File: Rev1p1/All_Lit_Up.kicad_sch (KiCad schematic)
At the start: 81 parts, among them U1 MCP1640BMC, U2 TLC555xPW

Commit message: Improved 1p1 Design
Cleaned up design, removed DFN for SOIC. added BOM, Schematic, & Step Files. reduced size to 100mm x 100mm. improved traces & Vias.
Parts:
- removed U1: MCP1640BMC, Package_DFN_QFN:DFN-8-1EP_3x2mm_P0.5mm_EP1.75x1.45mm, symbol ERW_Power:MCP1640BMC
- added G1: LOGO, ERW_LOGO:RuralguruProjects_HEX_2000, symbol ERW_LOGO:LOGO
- added G2: Phillip_LOGO, ERW_LOGO:PJ_LOGO_1p5l, symbol ERW_LOGO:Phillip_LOGO
- added G3: Logo_Open_Hardware_Small, Symbol:OSHW-Symbol_6.7x6mm_SilkScreen, symbol Graphic:Logo_Open_Hardware_Small
- added U1: MCP1640Bx-xCHY, Package_TO_SOT_SMD:SOT-23-6, symbol Regulator_Switching:MCP1640Bx-xCHY
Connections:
- net GND: now also U1.2 (GND)
- net PWR_EN: now also U1.3 (EN)
- net SWITCHER: now also U1.1 (SW)
- net VCC: now also U1.5 (V_{OUT})
- net V_{BAT}: now also U1.6 (V_{IN})
- net VFB renamed V_{FB}
- net V_{FB}: now also U1.4 (V_{FB})
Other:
- moved on the sheet: C1, C10, C13, C14, C16, C17, C2, C21, C23, C24, C25, C26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

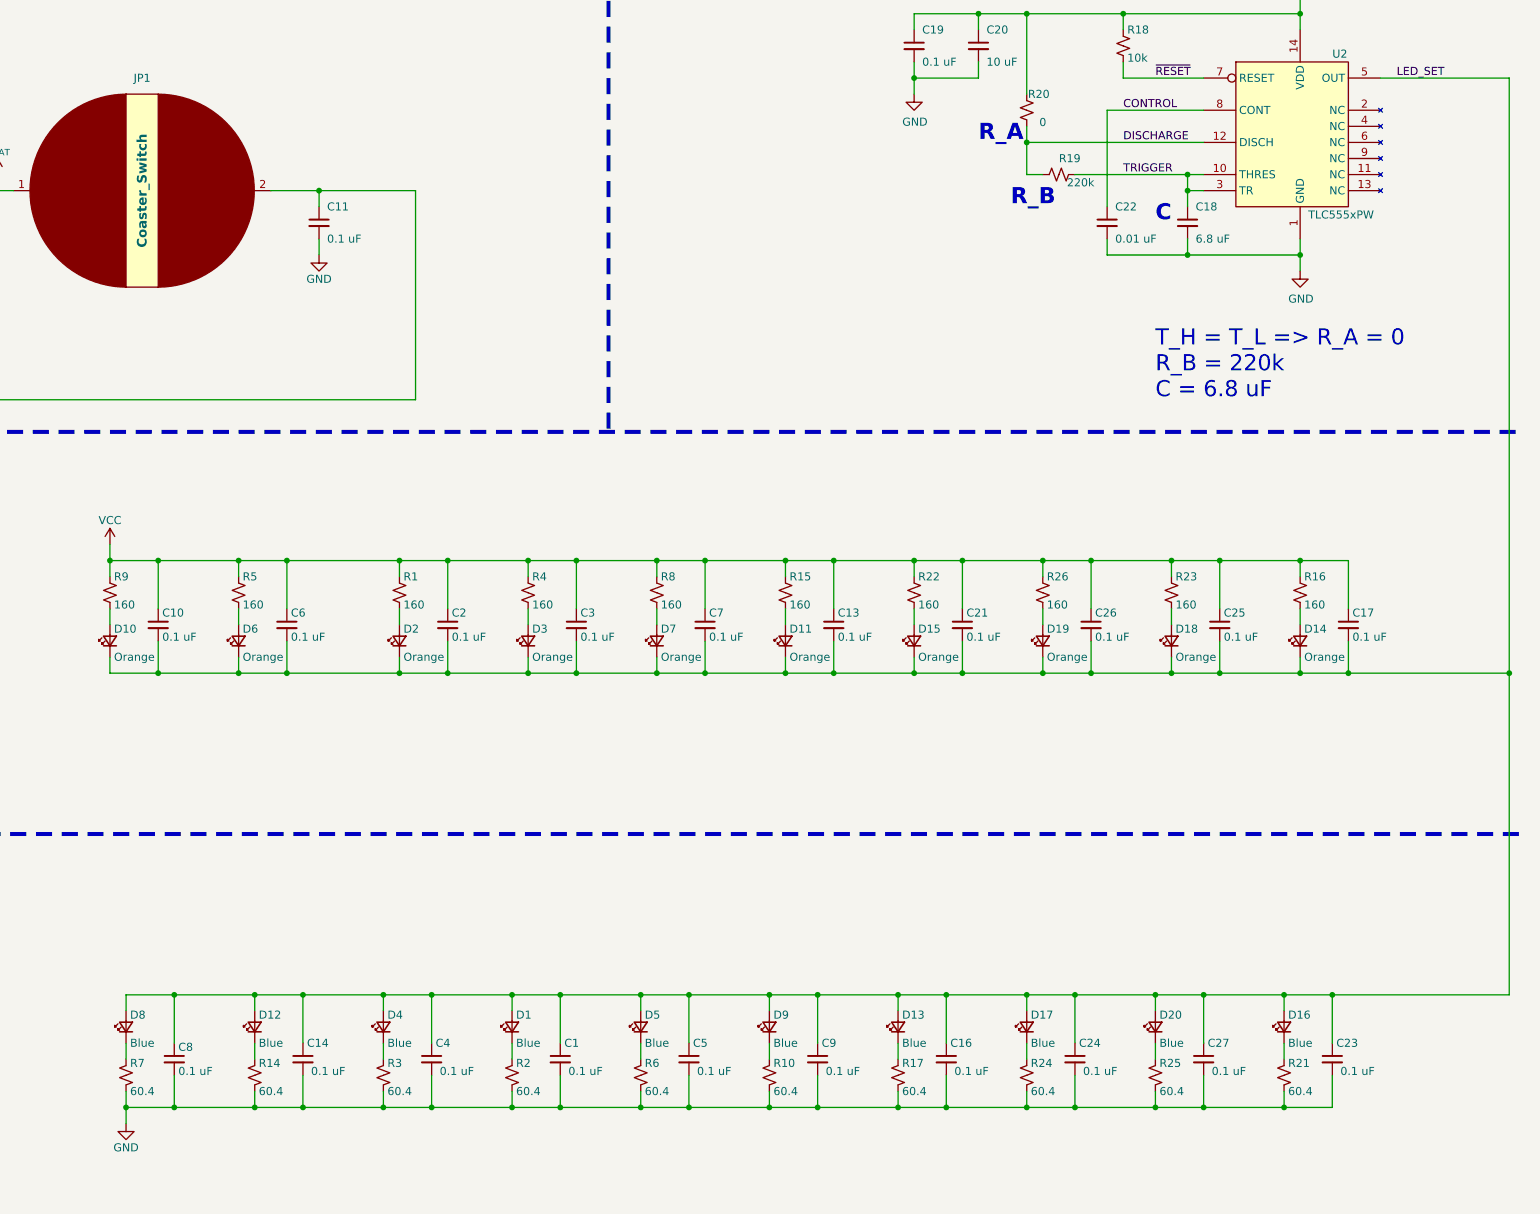
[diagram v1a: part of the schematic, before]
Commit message: Update to working model
Change LEDs to used Value, Correct to 1k, change resistor values to used. Add LED choice and orientation with silk. correct silk for 1 LED Cap combo. update gbrs. update output documents. Added iBOM
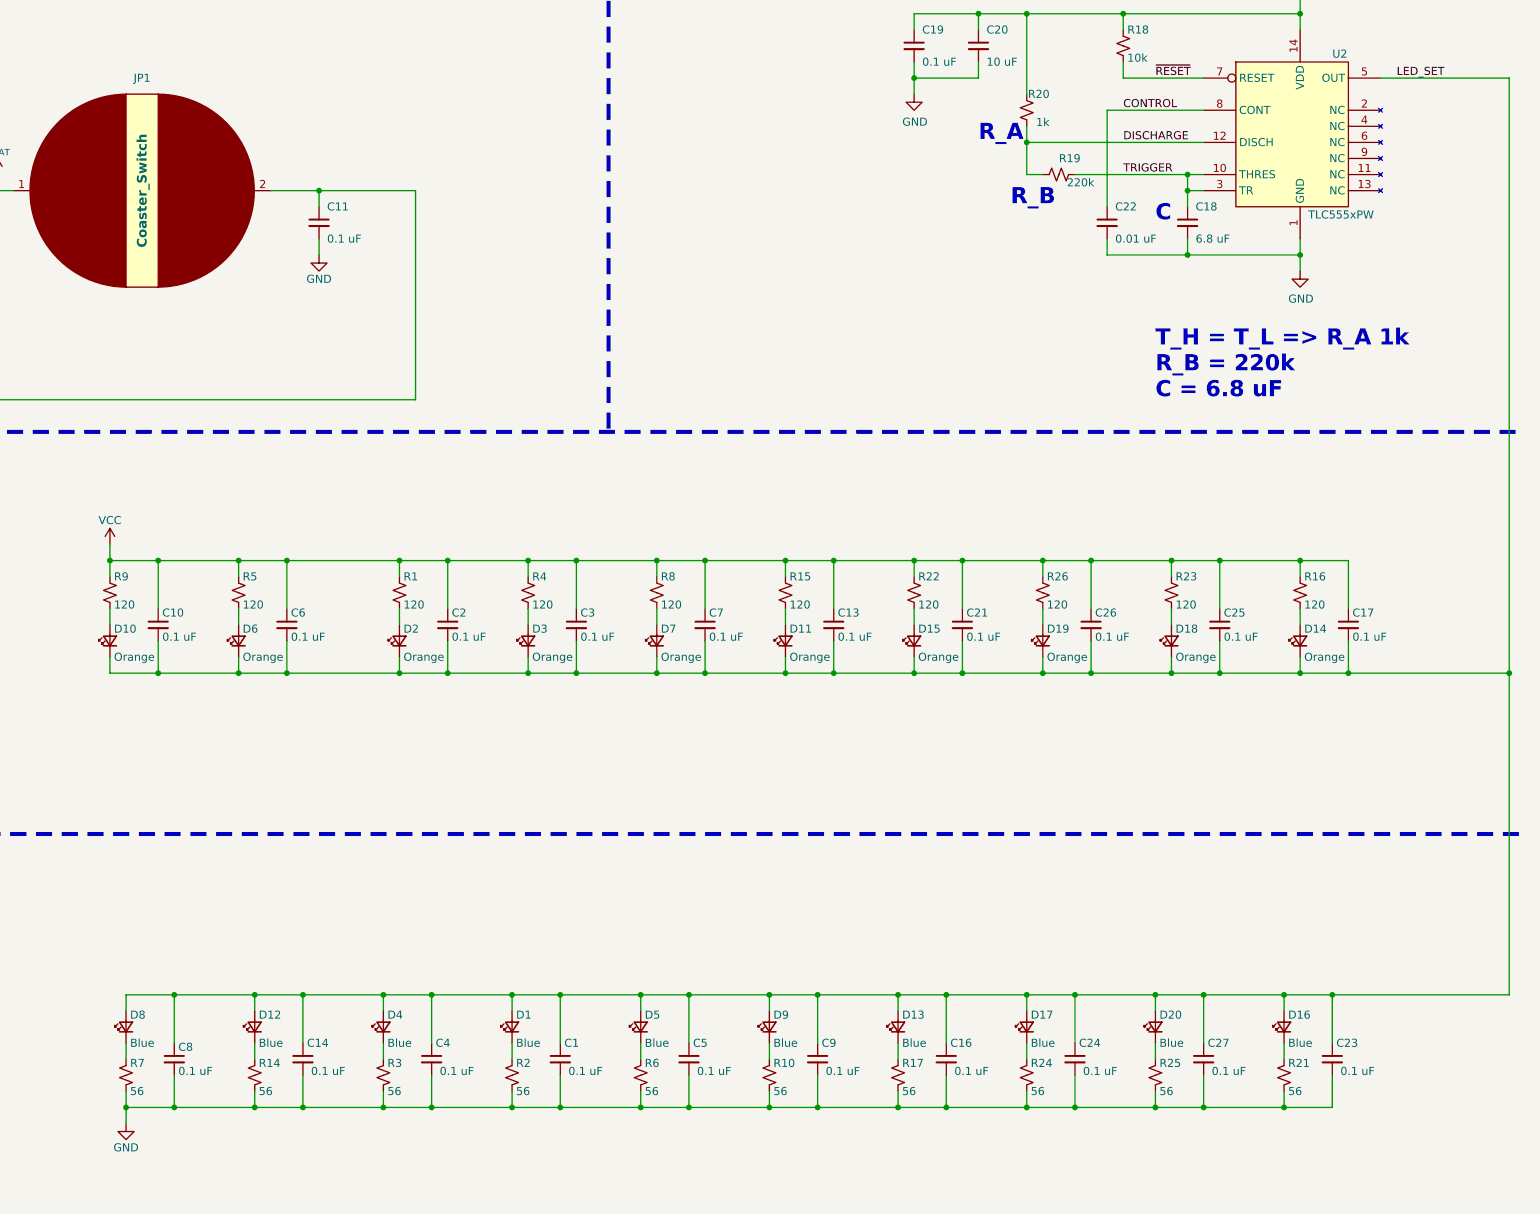
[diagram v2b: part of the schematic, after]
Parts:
- D1, D12, D13, D16, D17, D20, D4, D5, D8, D9: MFR Kingbright -> Harvatek Corporation; MPN APT1608VBC/D -> E1221NB--05D000814U1930; VPN 754-1789-1-ND -> 3147-E1221NB--05D000814U1930CT-ND
- D10, D11, D14, D15, D18, D19, D2, D3, D6, D7: MFR Kingbright -> Harvatek Corporation; MPN AP1608SECK -> B1911UD--20D001014U1930; VPN 754-AP1608SECKCT-ND -> 3147-B1911UD--20D001014U1930CT-ND
- G2, G3: MFR (none) -> -; MPN (none) -> -; VPN (none) -> -; Vendor (none) -> -
- R1, R15, R16, R22, R23, R26, R4, R5, R8, R9: value 160 -> 120; MFR Stackpole Electronics Inc -> Yageo; MPN RMCF0603FT160R -> RT0603FRE07120RL; VPN RMCF0603FT160RCT-ND -> 13-RT0603FRE07120RLCT-ND
- R10, R14, R17, R2, R21, R24, R25, R3, R6, R7: value 60.4 -> 56; MFR Panasonic Industry -> Yageo; MPN ERJ-3EKF60R4V -> RT0603FRE0756RL; VPN P60.4HCT-ND -> 13-RT0603FRE0756RLCT-ND
- R20: value 0 -> 1k; MFR YAGEO -> Yageo; MPN RC0603FR-070RL -> RT0603FRE131KL; VPN 311-0.0HRCT-ND -> 13-RT0603FRE131KLCT-ND
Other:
- note added: "T_H = T_L => R_A 1k R_B = 220k C = 6.8 uF"
- note removed: "T_H = T_L => R_A = 0 R_B = 220k C = 6.8 uF"
